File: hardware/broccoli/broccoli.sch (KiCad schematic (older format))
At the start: 83 parts, among them J1 PCB Antenna, J2 USB-MICRO-B, P1 DIGITAL, P11 SCLK, P12 SDAT, P2 PROGRAM, P3 JTAG, P4 EXPAND, P5 ANALOG, P6 VCC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

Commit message: started Broccoli/CC2400 contingency schematic
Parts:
- removed C1, C3: 1pF, symbol C
- removed C11: 1µF, 0603, symbol C
- removed C12, C5, C6, C7: 22pF, 0603, symbol C
- removed C4: 2n2, symbol C
- removed C8: 100nF, 0603, symbol C
- removed L2: 3n9, symbol INDUCTOR
- removed U2: TRC104, symbol TRC104
- added C?: 5p6, symbol C
- added C? (x2): 0p5, symbol C
- added C? (x4): 100nF, symbol C
- added C? (x3): 68nF, symbol C
- added C?: 10nF, symbol C
- added L? (x2): 7n5, symbol INDUCTOR
- added L?: 27nH, symbol INDUCTOR
- added R?: 43k, symbol R
- added U?: CC2400, symbol CC2400
- C10, C9: value 33pF -> 27pF; Field2 C1608C0G1H330JT -> C1608C0G1H270J; Field3 Multilayer Ceramic Capacitors (MLCC) - SMD/SMT 0603 33pF 50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 -> Multilayer Ceramic Capacitors (MLCC) - SMD/SMT 0603 27pF 50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
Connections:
- net labels added: 1V8, GIO1
- wire segments 313 -> 346
- no-connect marks 11 -> 15
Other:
- note added: "todo:\ngio1/clock\n1v8 regulator\ntest points\n0402 part selection\natest"
- moved on the sheet: BT1, C13, C14, C2, C25, C26, C27, C28, C29, C30, C32, C33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

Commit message: Broccoli/CC2400: added 1V8 regulator, clock distribution, big cap for power switching
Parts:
- removed C32, C35: 33pF, 0603, symbol C
- removed X2: MCU XTAL, symbol CRYSTAL
- added C?: 220pF, symbol C
- added C?: 100pF, symbol C
- added C?: 100µF, symbol C
- added C? (x2): 1µF, 0603, symbol C
- added D?: RSTLED, 0603D, symbol LED
- added R?: 10k, 0603, symbol R
- added R?: 330, 0603, symbol R
- added U?: PT7M8206, symbol TCR5SB
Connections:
- net +1.8V: now also C?.1, U?.5 (VOUT)
- net GIO1: now also C?.2
- net GND: now also C?.2, C?.2, C?.2, C?.2, D?.2 (K), R?.1, U?.2 (GND)
- net VCC: now also C?.1, C?.1, U?.1 (VIN)
- net at U4.19 (XTAL1): now also C?.1, C?.1
- net at U4.76 (P1[0]/ENET_TXD0): now also R?.2, R?.2, U?.3 (CTRL)
- new net: D?.1 (A), R?.1
- no-connect marks 15 -> 16
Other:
- note added: "todo:\ntest points\n0402 part selection\natest"
- note removed: "todo:\ngio1/clock\n1v8 regulator\ntest points\n0402 part selection\natest"
- moved on the sheet: BT1, C2, C25, C29, D16, Q2, R1, U1

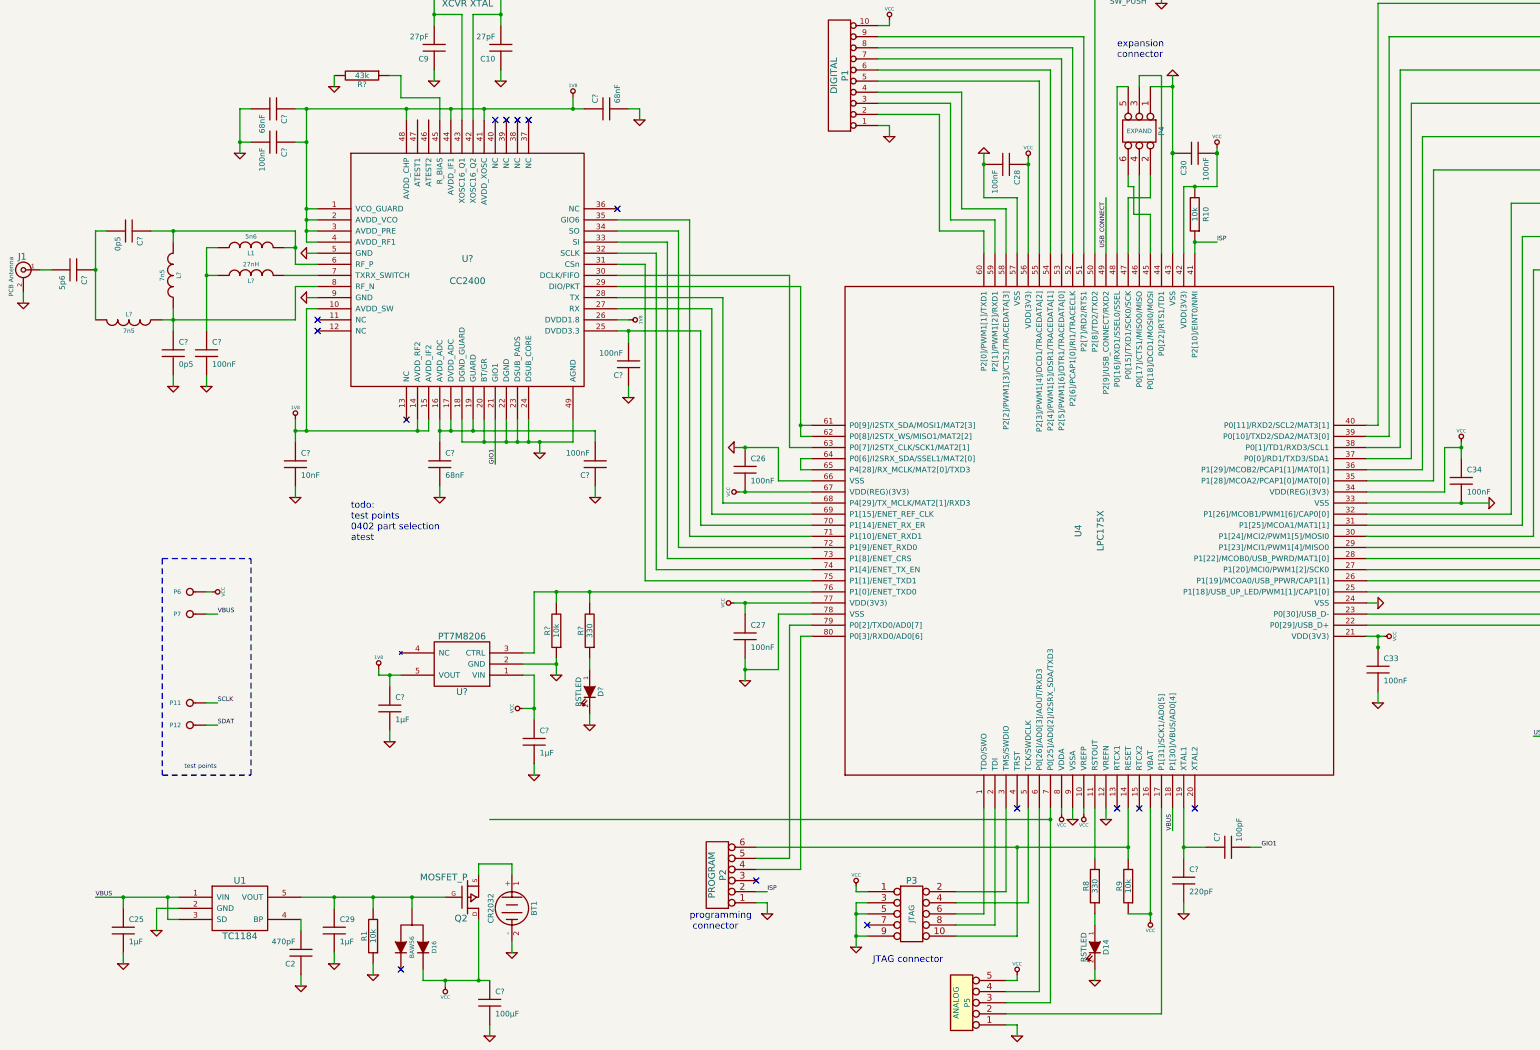
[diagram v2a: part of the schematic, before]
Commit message: Broccoli/CC2400: ATEST connections, test points, fixed missing 1V8 supply on CC2400
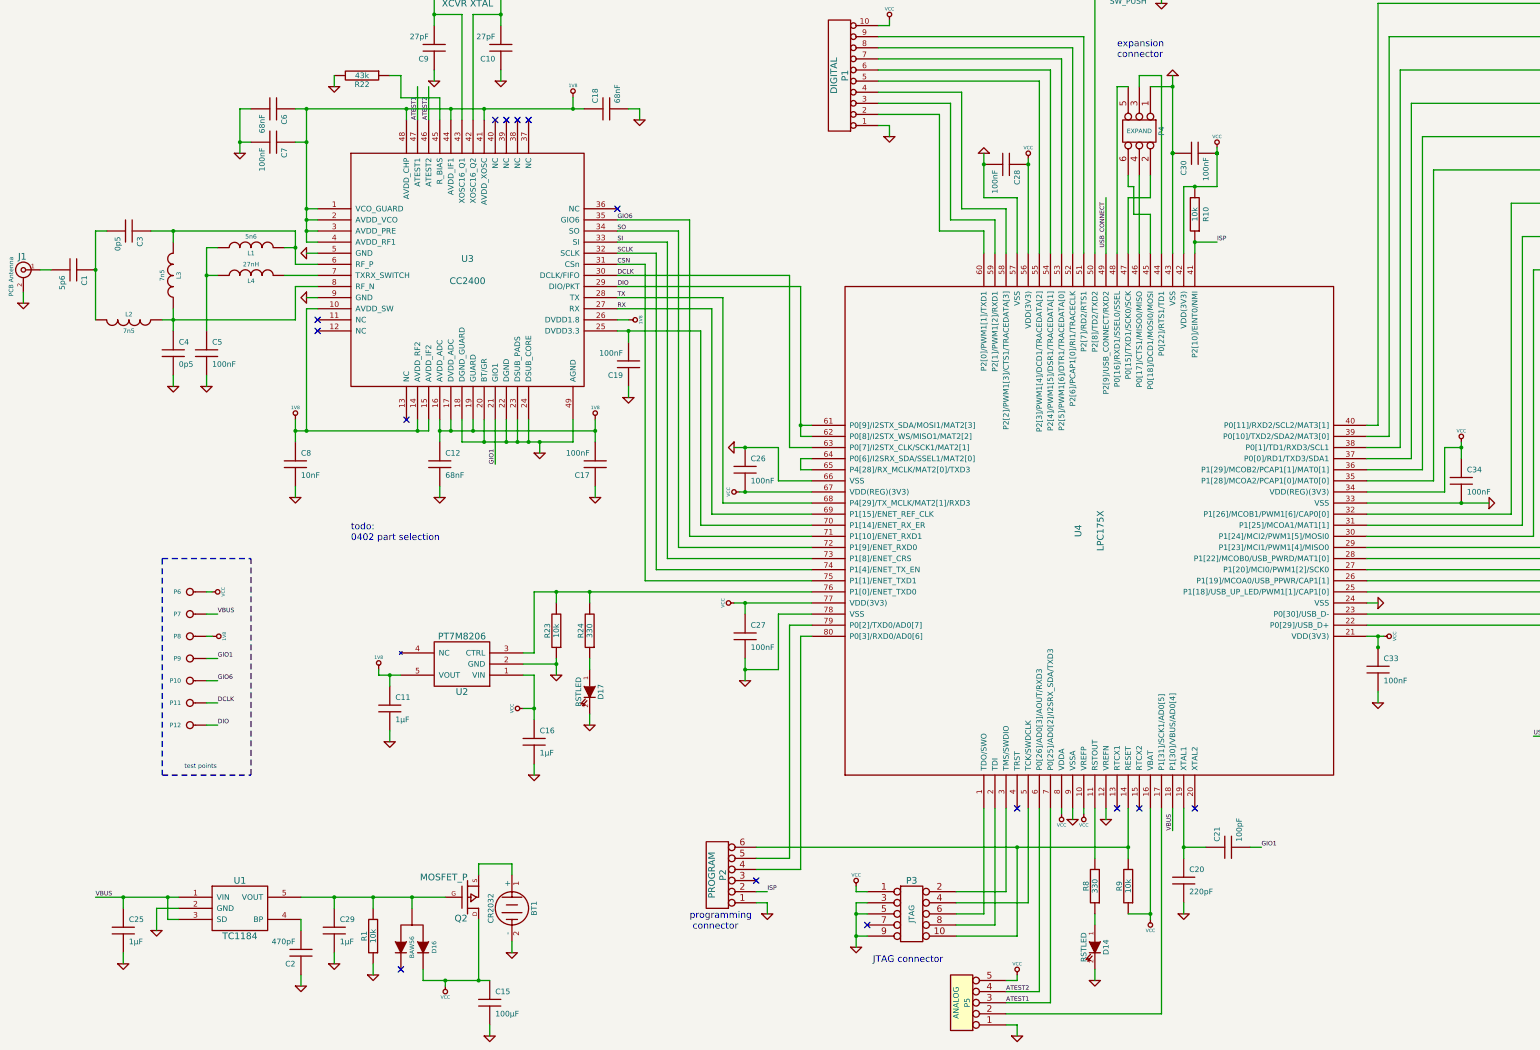
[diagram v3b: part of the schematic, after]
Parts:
- added P10: GIO6, testpad-50mil, symbol CONN_1
- added P8: 1V8, testpad-50mil, symbol CONN_1
- added P9: GIO1, testpad-50mil, symbol CONN_1
- P11: value SCLK -> DCLK
- P12: value SDAT -> DIO
- gave numbers to parts that had none: 25
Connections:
- net SDAT is gone; now on net DIO: P12.1
- net +1.8V: now also C12.1, C17.2, U3.16 (AVDD_ADC), U3.17 (DVDD_ADC), U3.19 (GUARD), P8.1
- net GIO1: now also P9.1
- net SCLK: now also U3.32 (SCLK), U4.74 (P1[4]/ENET_TX_EN); no longer P11.1
- net ATEST2: now reaches P5.4, U4.6 (P0[26]/AD0[3]/AOUT/RXD3)
- net ATEST2: now also U3.46 (ATEST2)
- net DIO: now reaches U3.29 (DIO/PKT), U4.61 (P0[9]/I2STX_SDA/MOSI1/MAT2[3]), U4.62 (P0[8]/I2STX_WS/MISO1/MAT2[2])
- net DCLK: now reaches U3.30 (DCLK/FIFO), U4.63 (P0[7]/I2STX_CLK/SCK1/MAT2[1])
- net DCLK: now also P11.1
- net TX: now reaches U3.28 (TX), U4.68 (P4[29]/TX_MCLK/MAT2[1]/RXD3)
- net RX: now reaches U3.27 (RX), U4.69 (P1[15]/ENET_REF_CLK)
- net ATEST1: now reaches P5.3, U4.7 (P0[25]/AD0[2]/I2SRX_SDA/TXD3)
- net ATEST1: now also U3.47 (ATEST1)
- net GIO6: now reaches U3.35 (GIO6), U4.71 (P1[10]/ENET_RXD1)
- net GIO6: now also P10.1
- net SO: now reaches U3.34 (SO), U4.72 (P1[9]/ENET_RXD0)
- net SI: now reaches U3.33 (SI), U4.73 (P1[8]/ENET_CRS)
- net CSN: now reaches U3.31 (CSn), U4.75 (P1[1]/ENET_TXD1)
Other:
- note added: "todo:\n0402 part selection"
- note removed: "todo:\ntest points\n0402 part selection\natest"

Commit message: Broccoli/CC2400: minor schematic/BOM tweaks
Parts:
- D14, D17: Field4 (none) -> DNP
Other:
- note added: "1V8 supply for CC2400"
- note added: "3V supply switches between battery and USB\npower depending on bus power availability"
- note added: "C15 optional to reduce glitch when\nswitching from USB to battery power"
- note added: "D14 not populated\n(to save power)"
- note added: "D17 not populated\n(to save power)"
- note added: "Ubertooth\nexpansion\nconnector"
- note added: "analog expansion port"
- note added: "digital expansion port"
- note removed: "expansion\nconnector"
- moved on the sheet: C4

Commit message: Broccoli/CC2400: BOM updates
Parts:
- C1: Field1 (none) -> TDK; Field2 (none) -> C1005C0G1H5R6D; Field3 (none) -> CAP CER 5.6PF 50V C0G 0402
- C21: Field3 Multilayer Ceramic Capacitors (MLCC) - SMD/SMT 0603 100pF 50volts C0G 5%Multilayer Ceramic Capacitors (MLCC) - SMD/SMT 0603 100pF 50volts C0G 5%Multilayer Ceramic Capacitors (MLCC) - SMD/SMT 0603 100pF 50volts C0G 5% -> Multilayer Ceramic Capacitors (MLCC) - SMD/SMT 0603 100pF 50volts C0G 5%
- C3, C4: Field1 (none) -> TDK; Field2 (none) -> C1005C0G1H0R5C; Field3 (none) -> CAP CER .5PF 50V C0G 0402
- L1: Field1 Kemet -> Johanson Technology; Field2 L0402C5N6SRMST -> L-07C5N6SV6T; Field3 RF Inductors 5.6nH 300mA 0.3nH -> CER INDUCTOR 5.6NH 0402
- L2, L3: Field1 (none) -> Johanson Technology; Field2 (none) -> L-07C7N5JV6T; Field6 (none) -> CER INDUCTOR 7.5NH 0402
- L4: Field1 Kemet -> TDK; Field2 L0402C5N6SRMST -> MLK1005S27NJ; Field3 RF Inductors 5.6nH 300mA 0.3nH -> INDUCTOR MULTILAYER 27NH 0402
- U4: Field2 LPC1754FBD80,551 -> LPC1752FBD80,551
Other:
- note removed: "todo:\n0402 part selection"
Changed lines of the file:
@@
-EESchema Schematic File Version 2  date Wed 24 Aug 2011 01:35:25 AM MDT
+EESchema Schematic File Version 2  date Wed 24 Aug 2011 03:38:46 PM MDT
 LIBS:ubertooth-symbols
 LIBS:power
@@
 Comment4 ""
 $EndDescr
+$Comp
+L C C4
+U 1 1 4E556A6E
+P 2800 4000
+F 0 "C4" H 2850 4100 50  0000 L CNN
+F 1 "0p5" H 2850 3900 50  0000 L CNN
+F 4 "TDK" H 2800 4000 60  0001 C CNN "Field1"
+F 5 "C1005C0G1H0R5C" H 2800 4000 60  0001 C CNN "Field2"
+F 6 "CAP CER .5PF 50V C0G 0402" H 2800 4000 60  0001 C CNN "Field3"
+	1    2800 4000
+	1    0    0    -1
+$EndComp
+$Comp
+L INDUCTOR L3
+U 1 1 4E5563E1
+P 2050 3300
+F 0 "L3" V 2000 3300 40  0000 C CNN
+F 1 "7n5" V 2150 3300 40  0000 C CNN
+F 4 "Johanson Technology" V 2050 3300 60  0001 C CNN "Field1"
+F 5 "L-07C7N5JV6T" V 2050 3300 60  0001 C CNN "Field2"
+F 6 "CER INDUCTOR 7.5NH 0402" V 2050 3300 60  0001 C CNN "Field6"
+	1    2050 3300
+	-1   0    0    1
+$EndComp
 Text Notes 4050 6300 0    60   ~ 0
 1V8 supply for CC2400
@@
 F 4 "TDK" H 11550 8450 60  0001 C CNN "Field1"
 F 5 "C1608C0G1H101J" H 11550 8450 60  0001 C CNN "Field2"
-F 6 "Multilayer Ceramic Capacitors (MLCC) - SMD/SMT 0603 100pF 50volts C0G 5%Multilayer Ceramic Capacitors (MLCC) - SMD/SMT 0603 100pF 50volts C0G 5%Multilayer Ceramic Capacitors (MLCC) - SMD/SMT 0603 100pF 50volts C0G 5%" H 11550 8450 60  0001 C CNN "Field3"
+F 6 "Multilayer Ceramic Capacitors (MLCC) - SMD/SMT 0603 100pF 50volts C0G 5%" H 11550 8450 60  0001 C CNN "Field3"
 	1    11550 8450
 	0    -1   -1   0
@@
 $EndComp
 NoConn ~ 11250 8100
-Text Notes 3650 5700 0    60   ~ 0
-todo:\n0402 part selection
 Text Label 4950 5000 1    40   ~ 0
 GIO1
@@
 F 0 "L4" V 2700 3300 40  0000 C CNN
 F 1 "27nH" V 2850 3300 40  0000 C CNN
-F 4 "Kemet" V 2750 3300 60  0001 C CNN "Field1"
-F 5 "L0402C5N6SRMST" V 2750 3300 60  0001 C CNN "Field2"
-F 6 "RF Inductors 5.6nH 300mA 0.3nH" V 2750 3300 60  0001 C CNN "Field3"
+F 4 "TDK" V 2750 3300 60  0001 C CNN "Field1"
+F 5 "MLK1005S27NJ" V 2750 3300 60  0001 C CNN "Field2"
+F 6 "INDUCTOR MULTILAYER 27NH 0402" V 2750 3300 60  0001 C CNN "Field3"
 	1    2750 3300
 	0    -1   -1   0
-$EndComp
-$Comp
-L INDUCTOR L3
-U 1 1 4E4DA1A9
-P 2050 3300
-F 0 "L3" V 2000 3300 40  0000 C CNN
-F 1 "7n5" V 2150 3300 40  0000 C CNN
-	1    2050 3300
-	-1   0    0    1
 $EndComp
 $Comp
@@
 F 0 "L2" V 1600 3700 40  0000 C CNN
 F 1 "7n5" V 1750 3700 40  0000 C CNN
+F 4 "Johanson Technology" V 1650 3700 60  0001 C CNN "Field1"
+F 5 "L-07C7N5JV6T" V 1650 3700 60  0001 C CNN "Field2"
+F 6 "CER INDUCTOR 7.5NH 0402" V 1650 3700 60  0001 C CNN "Field6"
 	1    1650 3700
 	0    1    1    0
@@
 F 0 "C3" H 1700 3000 50  0000 L CNN
 F 1 "0p5" H 1700 2800 50  0000 L CNN
+F 4 "TDK" H 1650 2900 60  0001 C CNN "Field1"
+F 5 "C1005C0G1H0R5C" H 1650 2900 60  0001 C CNN "Field2"
+F 6 "CAP CER .5PF 50V C0G 0402" H 1650 2900 60  0001 C CNN "Field3"
 	1    1650 2900
 	0    1    1    0
-$EndComp
-$Comp
-L C C4
-U 1 1 4E4DA15D
-P 2800 4000
-F 0 "C4" H 2850 4100 50  0000 L CNN
-F 1 "0p5" H 2850 3900 50  0000 L CNN
-	1    2800 4000
-	1    0    0    -1
 $EndComp
 $Comp
@@
 F 0 "C1" H 1200 3350 50  0000 L CNN
 F 1 "5p6" H 1200 3150 50  0000 L CNN
+F 4 "TDK" H 1150 3250 60  0001 C CNN "Field1"
+F 5 "C1005C0G1H5R6D" H 1150 3250 60  0001 C CNN "Field2"
+F 6 "CAP CER 5.6PF 50V C0G 0402" H 1150 3250 60  0001 C CNN "Field3"
 	1    1150 3250
 	0    1    1    0
@@
 F 2 "LQFP80" H 10300 5600 60  0001 C CNN
 F 4 "NXP" H 10300 5600 60  0001 C CNN "Field1"
-F 5 "LPC1754FBD80,551" H 10300 5600 60  0001 C CNN "Field2"
+F 5 "LPC1752FBD80,551" H 10300 5600 60  0001 C CNN "Field2"
 F 6 "Microcontrollers (MCU) ARM Cortex M3 Micro Controller" H 10300 5600 60  0001 C CNN "Field3"
 	1    10300 5600
@@
 F 0 "L1" V 2700 3050 40  0000 C CNN
 F 1 "5n6" V 2850 3050 40  0000 C CNN
-F 4 "Kemet" V 2750 3050 60  0001 C CNN "Field1"
-F 5 "L0402C5N6SRMST" V 2750 3050 60  0001 C CNN "Field2"
-F 6 "RF Inductors 5.6nH 300mA 0.3nH" V 2750 3050 60  0001 C CNN "Field3"
+F 4 "Johanson Technology" V 2750 3050 60  0001 C CNN "Field1"
+F 5 "L-07C5N6SV6T" V 2750 3050 60  0001 C CNN "Field2"
+F 6 "CER INDUCTOR 5.6NH 0402" V 2750 3050 60  0001 C CNN "Field3"
 	1    2750 3050
 	0    -1   -1   0

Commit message: Broccoli/CC2400: BOM updates
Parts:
- D17: value RSTLED -> 1V8LED
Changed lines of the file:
@@
-EESchema Schematic File Version 2  date Wed 24 Aug 2011 03:38:46 PM MDT
+EESchema Schematic File Version 2  date Wed 24 Aug 2011 03:42:26 PM MDT
 LIBS:ubertooth-symbols
 LIBS:power
@@
 P 5800 7050
 F 0 "D17" H 5800 7150 50  0000 C CNN
-F 1 "RSTLED" H 5800 6950 50  0000 C CNN
+F 1 "1V8LED" H 5800 6950 50  0000 C CNN
 F 2 "0603D" H 5800 7050 60  0001 C CNN
 F 4 "Kingbright" H 5800 7050 60  0001 C CNN "Field1"

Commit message: Broccoli/CC2400: BOM updates
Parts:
- U3: Field1 (none) -> Texas Instruments; Field2 (none) -> CC2400; Field3 (none) -> IC RF TXRX 2.4GHZ LP 48-QFN
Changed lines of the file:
@@
-EESchema Schematic File Version 2  date Wed 24 Aug 2011 03:42:26 PM MDT
+EESchema Schematic File Version 2  date Wed 24 Aug 2011 04:00:09 PM MDT
 LIBS:ubertooth-symbols
 LIBS:power
@@
 F 0 "U3" H 4700 3350 60  0000 C CNN
 F 1 "CC2400" H 4700 3150 60  0000 C CNN
+F 4 "Texas Instruments" H 4700 3250 60  0001 C CNN "Field1"
+F 5 "CC2400" H 4700 3250 60  0001 C CNN "Field2"
+F 6 "IC RF TXRX 2.4GHZ LP 48-QFN" H 4700 3250 60  0001 C CNN "Field3"
 	1    4700 3250
 	1    0    0    -1
